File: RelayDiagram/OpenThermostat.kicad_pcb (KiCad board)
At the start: 2 copper layers, 162.6 x 102.4 mm, 91 parts, among them J1 Conn_01x08_Female, J2 Conn_01x15_Female, J3 Conn_01x15_Female, J4 Conn_01x09_Female, Q1 Q_NMOS_DGS, Q10 Q_NMOS_DGS, Q11 Q_NMOS_DGS, Q12 Q_NMOS_DGS, Q2 Q_NMOS_DGS, Q3 Q_NMOS_DGS, Q4 Q_NMOS_DGS, Q5 Q_NMOS_DGS, Q6 Q_NMOS_DGS, Q7 Q_NMOS_DGS, Q8 Q_NMOS_DGS, Q9 Q_NMOS_DGS, SW2 SW_Push, SW3 SW_Push, SW4 SW_Push, SW5 SW_Push, SW6 SW_Push, U1 PCF8574, U10 MB10S-13, U11 L7805CV, U2 LCD, U3 DHT11, U4 EE2-3TNU-L_DPDT_Relay, U5 EE2-3TNU-L_DPDT_Relay, U6 EE2-3TNU-L_DPDT_Relay, U7 EE2-3TNU-L_DPDT_Relay, U8 EE2-3TNU-L_DPDT_Relay, U9 EE2-3TNU-L_DPDT_Relay

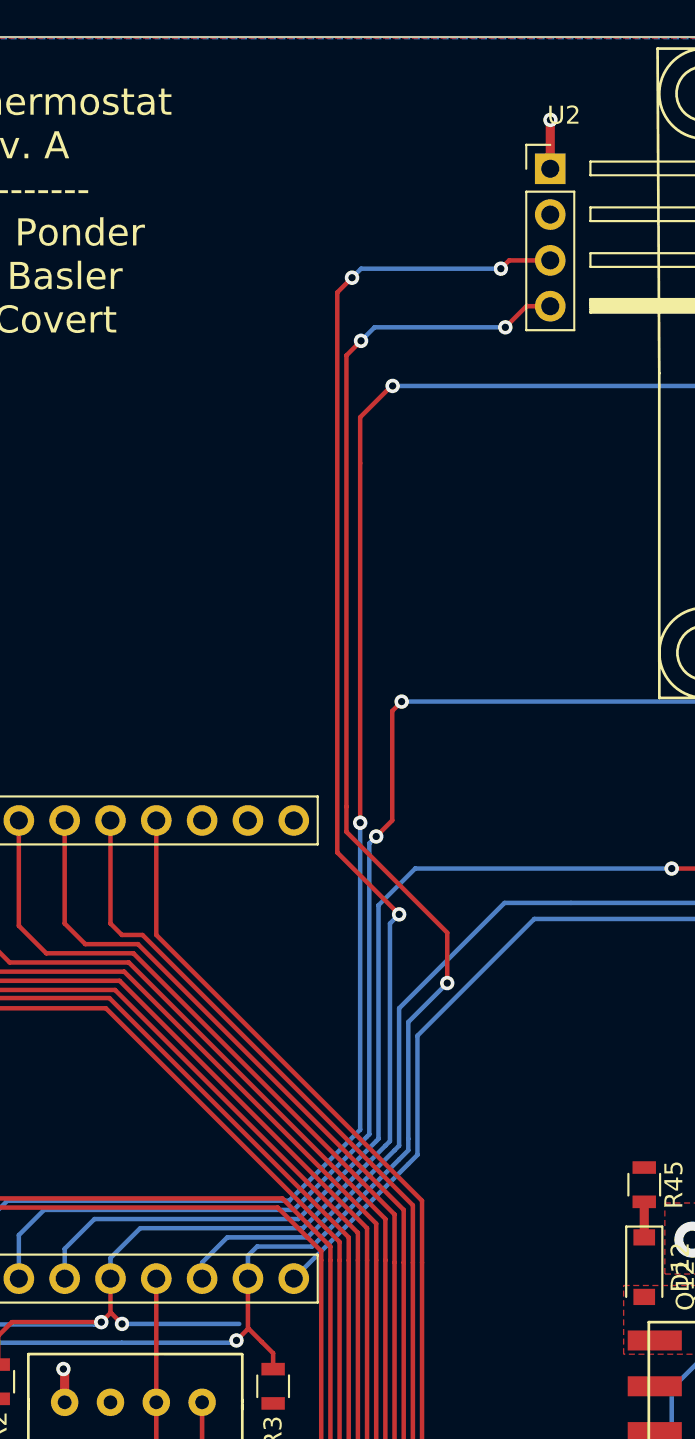
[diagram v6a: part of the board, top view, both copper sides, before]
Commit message: Moved 4 pin header for LCD
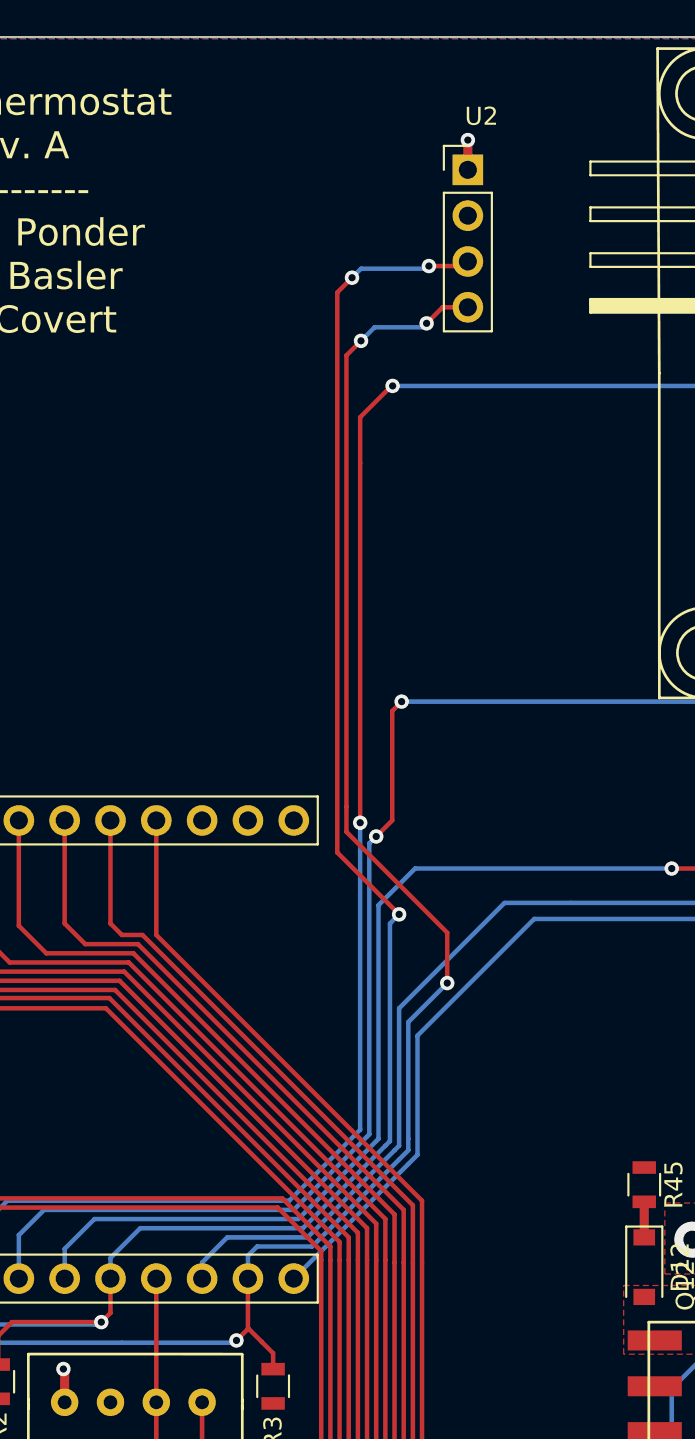
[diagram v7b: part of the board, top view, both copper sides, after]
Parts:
- moved U2 4.57 mm to (98.2, 64.8)
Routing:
- net Net-(J2-Pad11): track 119.6 -> 107.6 mm, vias 6 -> 5
- net Net-(J2-Pad14): track 106.0 -> 101.1 mm
- net GND: track 57.9 -> 56.9 mm
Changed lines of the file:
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@@
-(kicad_pcb (version 20171130) (host pcbnew "(5.0.0)")
+(kicad_pcb (version 20171130) (host pcbnew "(5.0.1)-3")
   (general
     (thickness 1.6)
     (drawings 25)
-    (tracks 667)
+    (tracks 663)
     (zones 0)
     (modules 91)
@@
   )
   (setup
-    (last_trace_width 0.762)
+    (last_trace_width 0.508)
     (user_trace_width 0.254)
     (user_trace_width 0.508)
@@
     (solder_mask_min_width 0.25)
     (aux_axis_origin 0 0)
-    (visible_elements 7FFFF7FF)
+    (visible_elements 7FFFFFFF)
     (pcbplotparams
       (layerselection 0x010fc_ffffffff)
@@
   )
   (module Pin_Headers:Pin_Header_Straight_1x04_Pitch2.54mm (layer F.Cu)
-    (at 102.74 64.71)
+    (at 98.171 64.77)
     (descr "Through hole straight pin header, 1x04, 2.54mm pitch, single row")
     (tags "Through hole pin header THT 1x04 2.54mm single row")
@@
   (segment (start 71.628 143.928998) (end 71.628 149.225) (width 0.254) (layer F.Cu) (net 32) (status 20))
   (segment (start 71.228001 143.528999) (end 71.628 143.928998) (width 0.254) (layer F.Cu) (net 32))
-  (via (at 102.75 62) (size 0.8) (drill 0.4) (layers F.Cu B.Cu) (net 34))
-  (segment (start 102.74 64.71) (end 102.74 62.01) (width 0.508) (layer F.Cu) (net 34))
-  (segment (start 102.74 62.01) (end 102.75 62) (width 0.508) (layer F.Cu) (net 34))
   (via (at 66.540277 139.785059) (size 0.8) (drill 0.4) (layers F.Cu B.Cu) (net 34))
   (segment (start 66.548 141.25) (end 66.548 139.792782) (width 0.508) (layer F.Cu) (net 34))
@@
   (via (at 198.247 102.616) (size 2) (drill 1) (layers F.Cu B.Cu) (net 34))
   (segment (start 197.231 103.632) (end 198.247 102.616) (width 1.016) (layer F.Cu) (net 34))
+  (via (at 98.171 63.119) (size 0.8) (drill 0.4) (layers F.Cu B.Cu) (net 34))
+  (segment (start 98.171 64.77) (end 98.171 63.119) (width 0.508) (layer F.Cu) (net 34))
   (segment (start 58.039 123.317) (end 59.563 121.793) (width 0.25) (layer F.Cu) (net 35))
   (segment (start 87.884 121.793) (end 59.563 121.793) (width 0.25) (layer F.Cu) (net 35))
@@
   (segment (start 78.359 128.143) (end 78.359 126.238) (width 0.25) (layer F.Cu) (net 38))
   (segment (start 77.851 128.651) (end 78.359 128.143) (width 0.25) (layer F.Cu) (net 38))
-  (via (at 79 128.75) (size 0.8) (drill 0.4) (layers F.Cu B.Cu) (net 38))
-  (segment (start 78.359 128.143) (end 78.393 128.143) (width 0.25) (layer F.Cu) (net 38))
-  (segment (start 78.393 128.143) (end 79 128.75) (width 0.25) (layer F.Cu) (net 38))
-  (segment (start 79 128.75) (end 85.500002 128.75) (width 0.25) (layer B.Cu) (net 38))
+  (segment (start 72.136 131.003) (end 72.136 129.413) (width 0.25) (layer F.Cu) (net 38) (status 400000))
+  (segment (start 72.898 128.651) (end 77.851 128.651) (width 0.25) (layer F.Cu) (net 38))
+  (segment (start 72.136 129.413) (end 72.898 128.651) (width 0.25) (layer F.Cu) (net 38))
   (via (at 91.75 70.75) (size 0.8) (drill 0.4) (layers F.Cu B.Cu) (net 38))
-  (segment (start 90.932 71.568) (end 91.75 70.75) (width 0.25) (layer F.Cu) (net 38))
+  (via (at 94.361 106.045) (size 0.8) (drill 0.4) (layers F.Cu B.Cu) (net 38))
   (segment (start 90.932 102.616) (end 90.932 71.568) (width 0.25) (layer F.Cu) (net 38))
+  (segment (start 90.932 71.568) (end 91.75 70.75) (width 0.25) (layer F.Cu) (net 38))
+  (segment (start 91.75 70.75) (end 92.25 70.25) (width 0.25) (layer B.Cu) (net 38))
   (segment (start 94.361 106.045) (end 90.932 102.616) (width 0.25) (layer F.Cu) (net 38))
-  (via (at 94.361 106.045) (size 0.8) (drill 0.4) (layers F.Cu B.Cu) (net 38))
-  (segment (start 93.853 106.553) (end 94.361 106.045) (width 0.25) (layer B.Cu) (net 38))
+  (segment (start 78.359 126.238) (end 78.359 125.095) (width 0.25) (layer B.Cu) (net 38) (status 400000))
   (segment (start 93.853 118.618) (end 93.853 106.553) (width 0.25) (layer B.Cu) (net 38))
   (segment (start 93.599 118.872) (end 93.853 118.618) (width 0.25) (layer B.Cu) (net 38))
-  (segment (start 78.359 125.095) (end 80.01 123.444) (width 0.25) (layer B.Cu) (net 38))
-  (segment (start 80.01 123.444) (end 89.027 123.444) (width 0.25) (layer B.Cu) (net 38))
   (segment (start 89.027 123.444) (end 93.599 118.872) (width 0.25) (layer B.Cu) (net 38))
-  (segment (start 78.359 126.238) (end 78.359 125.095) (width 0.25) (layer B.Cu) (net 38) (status 400000))
-  (segment (start 100 70.25) (end 100.46 69.79) (width 0.25) (layer F.Cu) (net 38))
-  (segment (start 100.46 69.79) (end 102.74 69.79) (width 0.25) (layer F.Cu) (net 38))
-  (segment (start 92.25 70.25) (end 100 70.25) (width 0.25) (layer B.Cu) (net 38))
-  (segment (start 91.75 70.75) (end 92.25 70.25) (width 0.25) (layer B.Cu) (net 38))
-  (via (at 100 70.25) (size 0.8) (drill 0.4) (layers F.Cu B.Cu) (net 38))
-  (segment (start 72.136 131.003) (end 72.136 129.413) (width 0.25) (layer F.Cu) (net 38) (status 400000))
-  (segment (start 72.898 128.651) (end 77.851 128.651) (width 0.25) (layer F.Cu) (net 38))
-  (segment (start 72.136 129.413) (end 72.898 128.651) (width 0.25) (layer F.Cu) (net 38))
+  (segment (start 80.01 123.444) (end 89.027 123.444) (width 0.25) (layer B.Cu) (net 38))
+  (segment (start 78.359 125.095) (end 80.01 123.444) (width 0.25) (layer B.Cu) (net 38))
+  (segment (start 93.853 106.553) (end 94.361 106.045) (width 0.25) (layer B.Cu) (net 38))
+  (via (at 96.012 70.104) (size 0.8) (drill 0.4) (layers F.Cu B.Cu) (net 38))
+  (segment (start 92.25 70.25) (end 95.866 70.25) (width 0.25) (layer B.Cu) (net 38))
+  (segment (start 95.866 70.25) (end 96.012 70.104) (width 0.25) (layer B.Cu) (net 38))
+  (segment (start 97.917 70.104) (end 98.171 69.85) (width 0.25) (layer F.Cu) (net 38))
+  (segment (start 96.012 70.104) (end 97.917 70.104) (width 0.25) (layer F.Cu) (net 38))
   (via (at 60.706 129.794) (size 0.8) (drill 0.4) (layers F.Cu B.Cu) (net 39))
   (segment (start 60.198 131.8) (end 60.198 130.302) (width 0.25) (layer F.Cu) (net 39))
@@
   (segment (start 85.979 129.032) (end 85.979 126.238) (width 0.25) (layer F.Cu) (net 39))
   (segment (start 85.344 129.667) (end 85.979 129.032) (width 0.25) (layer F.Cu) (net 39))
-  (segment (start 102.57 72.5) (end 102.74 72.33) (width 0.25) (layer F.Cu) (net 39))
   (segment (start 85.979 129.032) (end 86.032 129.032) (width 0.25) (layer F.Cu) (net 39))
   (segment (start 87.376 130.376) (end 86.75 129.75) (width 0.25) (layer F.Cu) (net 39))
@@
   (segment (start 91.44 101.473) (end 91.44 100.076) (width 0.25) (layer F.Cu) (net 39))
   (segment (start 85.979 126.238) (end 85.979 124.968) (width 0.25) (layer B.Cu) (net 39) (status 400000))
-  (via (at 100.25 73.5) (size 0.8) (drill 0.4) (layers F.Cu B.Cu) (net 39))
   (segment (start 92.25 74.25) (end 93 73.5) (width 0.25) (layer B.Cu) (net 39))
-  (segment (start 93 73.5) (end 100.25 73.5) (width 0.25) (layer B.Cu) (net 39))
-  (segment (start 101.42 72.33) (end 102.74 72.33) (width 0.25) (layer F.Cu) (net 39))
-  (segment (start 100.25 73.5) (end 101.42 72.33) (width 0.25) (layer F.Cu) (net 39))
+  (via (at 95.885 73.279) (size 0.8) (drill 0.4) (layers F.Cu B.Cu) (net 39))
+  (segment (start 93 73.5) (end 95.664 73.5) (width 0.25) (layer B.Cu) (net 39))
+  (segment (start 95.664 73.5) (end 95.885 73.279) (width 0.25) (layer B.Cu) (net 39))
+  (segment (start 96.774 72.39) (end 98.171 72.39) (width 0.25) (layer F.Cu) (net 39))
+  (segment (start 95.885 73.279) (end 96.774 72.39) (width 0.25) (layer F.Cu) (net 39))
   (segment (start 94 76.75) (end 149 76.75) (width 0.25) (layer B.Cu) (net 40))
   (segment (start 93.938 76.75) (end 94 76.75) (width 0.25) (layer F.Cu) (net 40))

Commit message: MEETING CHANGES
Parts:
- added ?: , solarcar-misc:MountingHole_3.2mm_M3, F.Cu at (54.5, 156.3)
- added ?: , solarcar-misc:MountingHole_3.2mm_M3, F.Cu at (54.5, 60.8)
- added ?: , solarcar-misc:MountingHole_3.2mm_M3, F.Cu at (210.2, 60.8)
- added ?: , solarcar-misc:MountingHole_3.2mm_M3, F.Cu at (210.2, 156.3)
- moved R4 56.9 mm to (71.6, 81.5), turned to 270 degrees
- moved U3 54.3 mm to (63.9, 81.0)
- moved U2 11.4 mm to (86.7, 64.6)
- moved J1 6.11 mm to (77.7, 149.6)
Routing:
- net Net-(J2-Pad12): track 11.3 -> 65.3 mm, vias 0 -> 1
- net Net-(J1-Pad8): track 26.1 -> 31.7 mm
- net Net-(J1-Pad7): track 28.3 -> 33.4 mm
- net +5V: track 19.2 -> 14.7 mm, vias 4 -> 6
- net Net-(J1-Pad6): track 30.8 -> 34.7 mm
- net Net-(J1-Pad3): track 10.3 -> 14.2 mm
- net Net-(J1-Pad2): track 13.6 -> 17.2 mm
- net Net-(J1-Pad5): track 33.1 -> 36.7 mm
- net GND: track 56.9 -> 53.4 mm, vias 24 -> 22
- net Net-(J1-Pad1): track 17.5 -> 20.7 mm
- net Net-(J2-Pad11): track 107.6 -> 105.1 mm, vias 5 -> 3
- net Net-(J1-Pad4): track 8.33 -> 10.6 mm
- net Net-(J2-Pad14): track 101.1 -> 101.3 mm, vias 5 -> 4
